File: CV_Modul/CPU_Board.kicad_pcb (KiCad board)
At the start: 4 copper layers, 60 x 100 mm, 117 parts, among them J101 Screw_Terminal_01x03, J102 Conn_02x01, J103 Conn_02x01, J104 Conn_01x08_Male, J105 Conn_02x09_Odd_Even, J106 Micro_SD_Card_Det, J107 Conn_01x06_Male, J108 Conn_02x01, J109 Conn_02x01, J110 Screw_Terminal_01x04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

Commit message: stepper board fertig gestellt
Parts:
- added D105: SS22F-SS2200F, Diode_SMD:D_SMA, F.Cu at (87.7, 54.5)
- U1: value TJA1051T-3 -> SN65HVD230DR
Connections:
- J107 pad 6: Net-(J107-Pad6) -> (no net)
- J110 pad 1: +24V -> Net-(D105-Pad2)
- U101 pad 103: Net-(U101-Pad103) -> (no net)
- U101 pad 104: Net-(U101-Pad104) -> (no net)
- U101 pad 110: Net-(U101-Pad110) -> (no net)
- U101 pad 111: Net-(U101-Pad111) -> (no net)
- U101 pad 112: Net-(U101-Pad112) -> (no net)
- U101 pad 113: Net-(U101-Pad113) -> (no net)
- U101 pad 116: Net-(U101-Pad116) -> (no net)
- U101 pad 118: Net-(U101-Pad118) -> (no net)
- U101 pad 119: Net-(U101-Pad119) -> (no net)
- U101 pad 122: Net-(U101-Pad122) -> (no net)
- U101 pad 134: Net-(U101-Pad134) -> (no net)
- U101 pad 137: Net-(U101-Pad137) -> (no net)
- U101 pad 139: Net-(U101-Pad139) -> (no net)
- U101 pad 140: Net-(U101-Pad140) -> (no net)
- U101 pad 20: Net-(U101-Pad20) -> (no net)
- U101 pad 21: Net-(U101-Pad21) -> (no net)
- U101 pad 22: Net-(U101-Pad22) -> (no net)
- U101 pad 28: Net-(U101-Pad28) -> (no net)
- U101 pad 29: Net-(U101-Pad29) -> (no net)
- U101 pad 37: Net-(U101-Pad37) -> (no net)
- U101 pad 44: Net-(U101-Pad44) -> (no net)
- U101 pad 45: Net-(U101-Pad45) -> (no net)
- U101 pad 47: Net-(U101-Pad47) -> (no net)
- U101 pad 48: Net-(U101-Pad48) -> (no net)
- U101 pad 87: Net-(U101-Pad87) -> (no net)
- U101 pad 88: Net-(U101-Pad88) -> (no net)
- U101 pad 9: Net-(U101-Pad9) -> (no net)
- U101 pad 91: Net-(U101-Pad91) -> (no net)
- U101 pad 92: Net-(U101-Pad92) -> (no net)
- U101 pad 98: Net-(U101-Pad98) -> (no net)
- U102 pad 36: Net-(U102-Pad36) -> (no net)
- U102 pad 40: Net-(U102-Pad40) -> (no net)
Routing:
- net Net-(U101-Pad104): track 65.5 -> 0.00 mm, vias 2 -> 0
- net Net-(U101-Pad103): track 64.1 -> 0.00 mm, vias 2 -> 0
- net Net-(U101-Pad98): track 60.6 -> 0.00 mm, vias 2 -> 0
- net /PA14: track 110.5 -> 108.6 mm
- net /PA13: track 100.0 -> 101.7 mm
- added copper zone on F.Cu, net Net-(D105-Pad2)

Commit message: Controller Board geplaced
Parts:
- L1: footprint Inductor_SMD:L_CommonModeChoke_Coilcraft_1812CAN -> ProjectFootprints:L_CommonModeChoke_Coilcraft_1812CAN
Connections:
- L1 pad 1: /CAN_H -> Net-(L1-Pad1)
- L1 pad 2: Net-(L1-Pad2) -> /CAN_H
- R6 pad 2: Net-(L1-Pad2) -> Net-(L1-Pad1)
- U1 pad 7: Net-(L1-Pad2) -> Net-(L1-Pad1)
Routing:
- net Net-(L1-Pad2): track 5.73 -> 0.00 mm
- net Net-(L1-Pad1): track 0.00 -> 5.73 mm

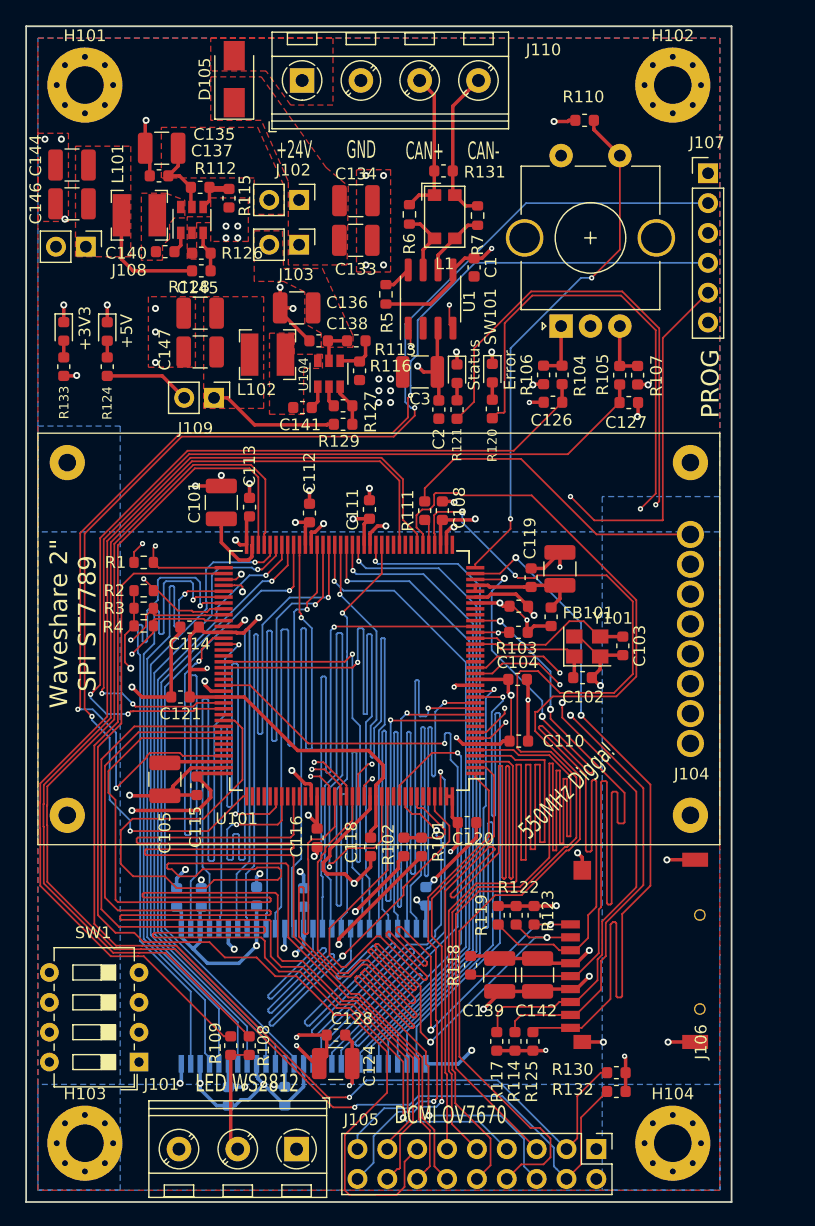
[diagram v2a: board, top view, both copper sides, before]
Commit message: Controller Modul und CV Modul Can schaltung berichtigt. CV Modul abgerundete Ecken r=5mm. TODO: IO Modul, Feeder-Steckplätze, Display Modul
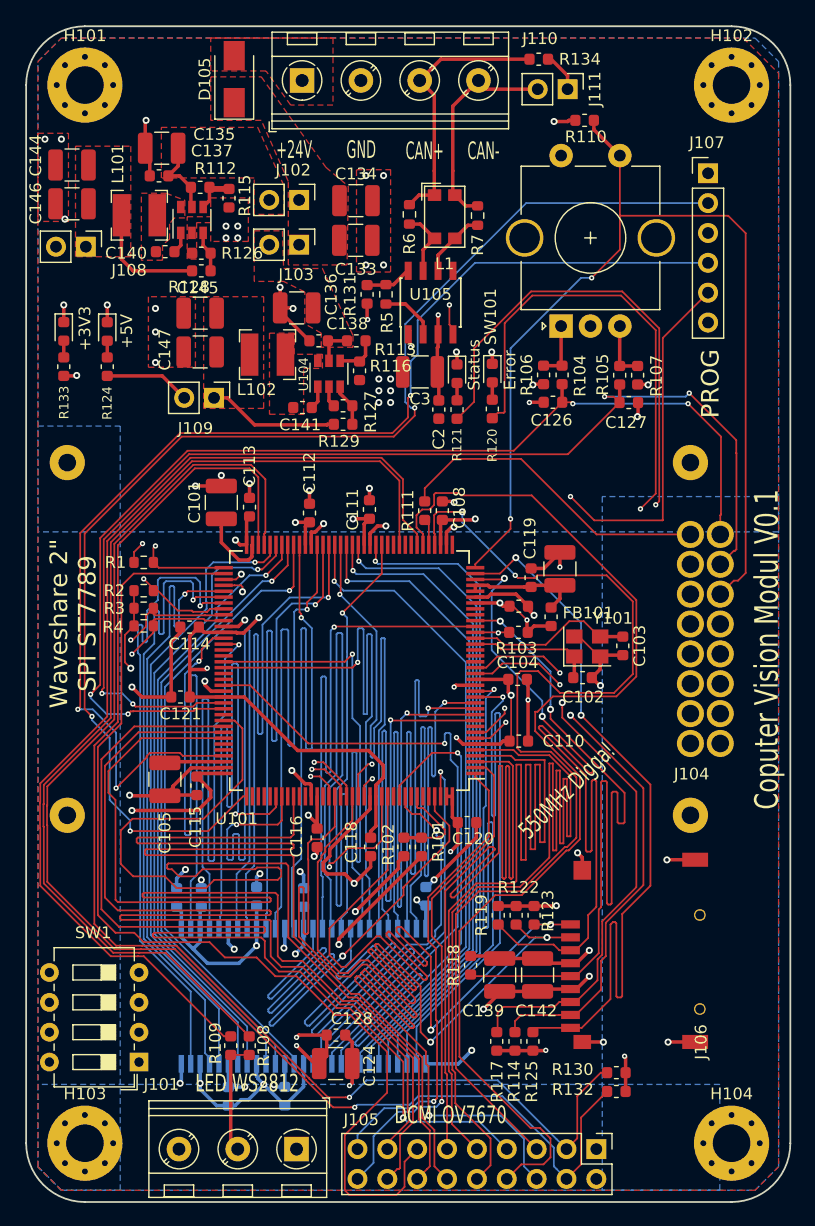
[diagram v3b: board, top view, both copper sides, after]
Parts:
- removed C1: 100n, Capacitor_SMD:C_0603_1608Metric
- removed U1: SN65HVD230DR, Package_SO:SOIC-8_3.9x4.9mm_P1.27mm
- added J111: Conn_02x01, Connector_PinHeader_2.54mm:PinHeader_1x02_P2.54mm_Vertical, F.Cu at (116.0, 55.4)
- added R134: 120R, Resistor_SMD:R_0603_1608Metric, F.Cu at (113.6, 52.8)
- added U105: SN65HVD230, Package_SO:SOIC-8_3.9x4.9mm_P1.27mm, F.Cu at (104.4, 73.5)
- R131: value 100R -> 10K
- moved R131 12.3 mm to (99.0, 72.8), turned to 90 degrees
- moved H102 5.00 mm to (130.0, 55.0)
- moved H104 5.00 mm to (130.0, 145.0)
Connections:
- C2 pad 1: +5V -> +3V3
- C3 pad 1: +5V -> +3V3
- R131 pad 1: /CAN_H -> +3V3
- R131 pad 2: /CAN_L -> Net-(R131-Pad2)
- R5 pad 1: +3V3 -> GND
- R5 pad 2: Net-(R5-Pad2) -> Net-(R131-Pad2)
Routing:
- net /PA2: track 44.6 -> 87.7 mm
- net +5V: track 112.9 -> 84.1 mm, vias 3 -> 2
- net /PC6: track 74.3 -> 100.0 mm, vias 2 -> 4
- net /PC7: track 71.6 -> 94.7 mm, vias 2 -> 4
- net /CAN_H: track 12.7 -> 22.8 mm
- net /CAN_L: track 13.0 -> 18.4 mm
- net GND: track 174.5 -> 179.4 mm
- net Net-(R131-Pad2): track 0.00 -> 4.03 mm
- net Net-(J111-Pad1): track 0.00 -> 3.39 mm
- net +3V3: track 188.2 -> 185.1 mm, vias 30 -> 31
- net Net-(R5-Pad2): track 2.41 -> 0.00 mm
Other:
- board size 60 x 100 mm -> 65 x 100 mm
- board text added: "Coputer Vision Modul V0.1"

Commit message: Leere Symbole mit leeren Footprints hinzugefügt für BOM export
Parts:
- added J112: IPC 16P, ProjectFootprints:Empty, F.Cu at (130.0, 129.0)
- added U106: IDC Connector 18P, ProjectFootprints:Empty, F.Cu at (130.0, 130.0)
- added U107: IDC Connector 18P, ProjectFootprints:Empty, F.Cu at (130.0, 128.0)
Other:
- board text added: "Empty Footprints for BOM"

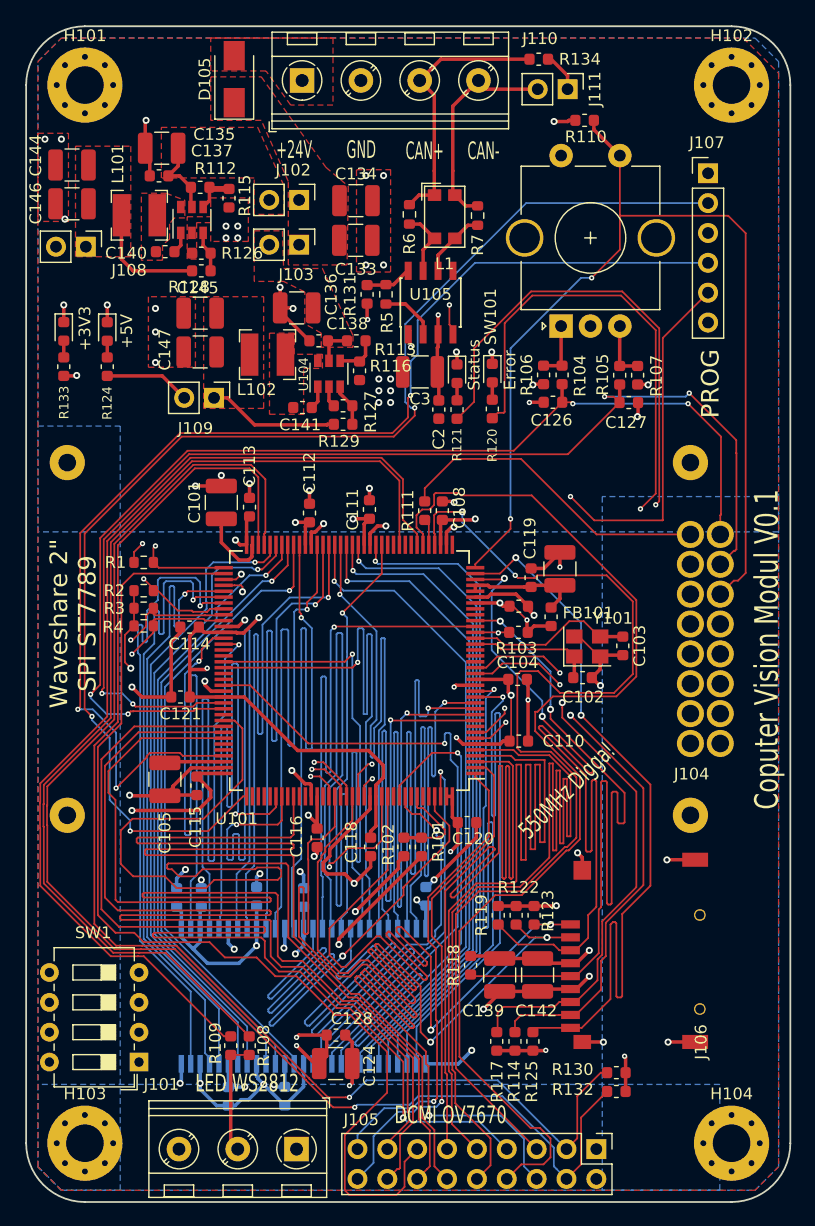
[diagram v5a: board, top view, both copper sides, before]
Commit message: CV Modul Reset Button hinzugefügt
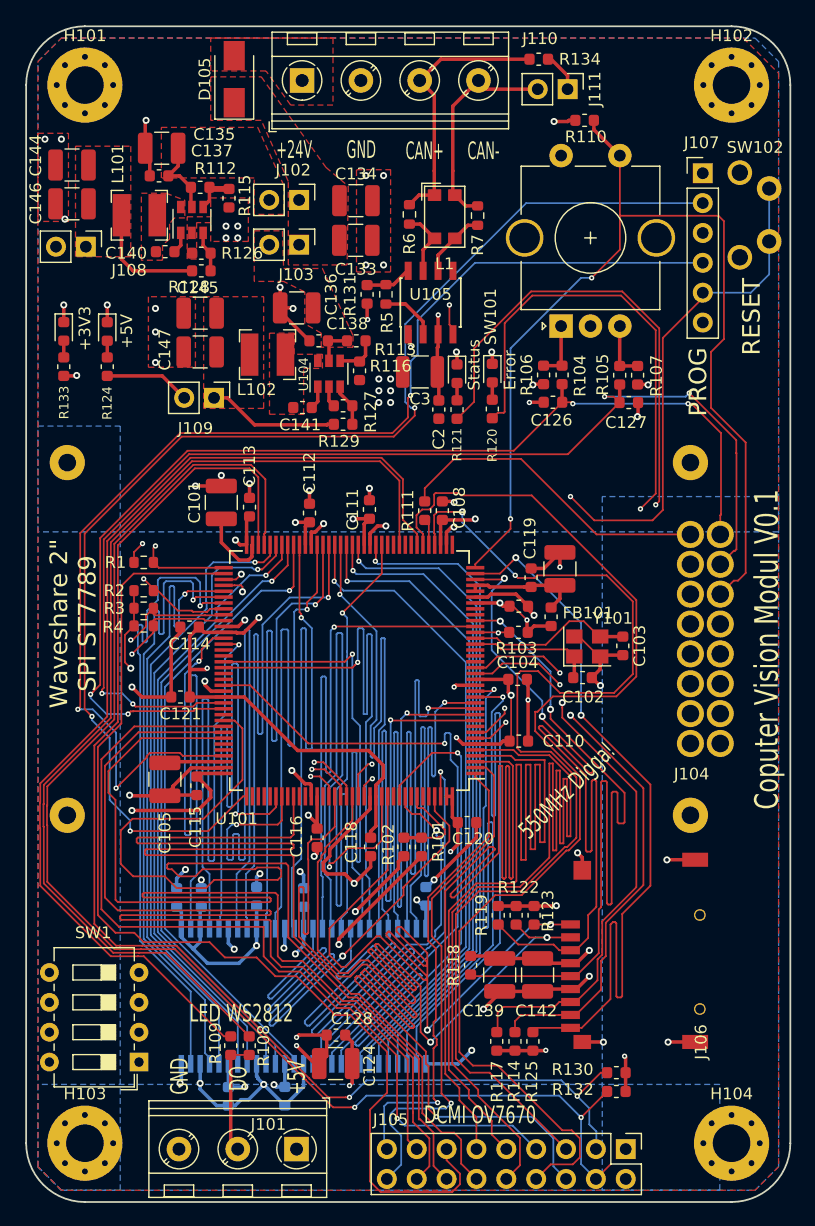
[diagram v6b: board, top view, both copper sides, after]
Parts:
- added SW102: SW_Push, ProjectFootprints:TactileSwitchLCSC, F.Cu at (133.2, 66.0)
- moved J105 2.50 mm to (121.0, 145.5)
- moved J107 0.45 mm to (127.5, 62.5)
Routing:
- net /CAM_XCLK: track 90.1 -> 74.4 mm
- net /NRST: track 46.9 -> 60.0 mm
- net /CAM_PCLK: track 96.2 -> 98.4 mm
- net /CAM_VSYNC: track 82.8 -> 85.0 mm
- net /CAM_HSYNC: track 94.2 -> 96.2 mm
- net /CAM_D5: track 89.7 -> 91.4 mm
- net /CAM_RESET: track 43.4 -> 44.6 mm
- net /CAM_D7: track 89.4 -> 90.5 mm
- net /CAM_D4: track 89.1 -> 90.2 mm
- net /CAM_D6: track 90.6 -> 91.6 mm
- net /CAM_D2: track 90.0 -> 90.9 mm
- net /CAM_SIOD: track 111.4 -> 110.7 mm, vias 1 -> 2
- net /CAM_D0: track 90.0 -> 89.5 mm
- net /CAM_SIOC: vias 1 -> 2
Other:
- board text added: "DO"
- board text added: "RESET"
